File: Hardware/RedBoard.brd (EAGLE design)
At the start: 68.6 x 58.4 mm, 85 parts, among them IC3 LM1117, J2 ISP, J3 5.5x2.1mm Barrel, J4 QWIIC_RIGHT_ANGLE, J5 USB Female Type C Connector, Q1 20V/4.2A/52mΩ/1.4W, Q2 310mA/60V/1.6Ω, Q3 310mA/60V/1.6Ω, U3 3.3V, U4 ATMEGA328P_TQFP, U5 CH340C, Y1 16MHz

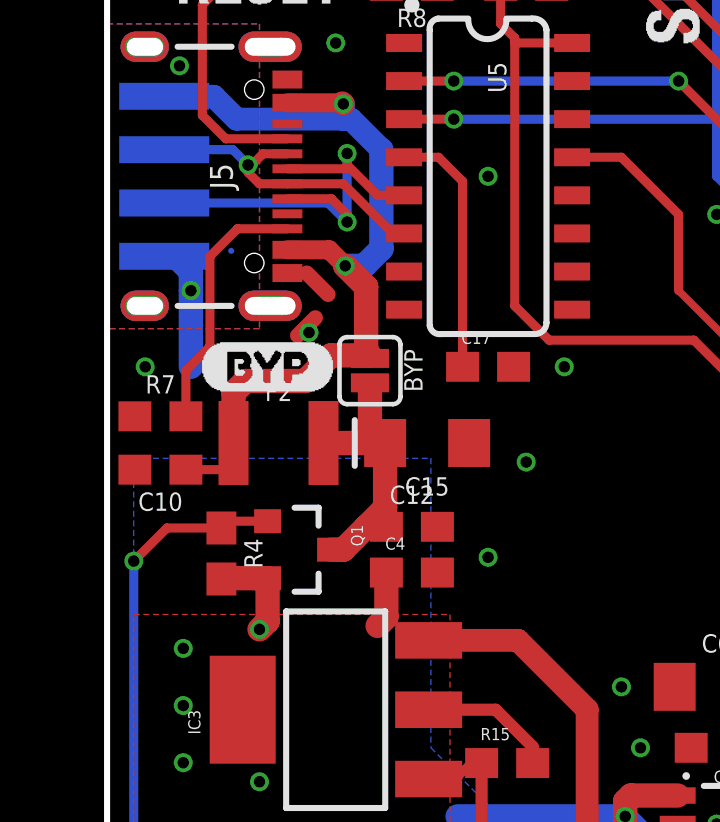
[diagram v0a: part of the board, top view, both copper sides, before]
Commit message: Go through DRC errors
Updated power MOSFET to be capable of 4.2A
Broke out A6 and A7 pins to headers
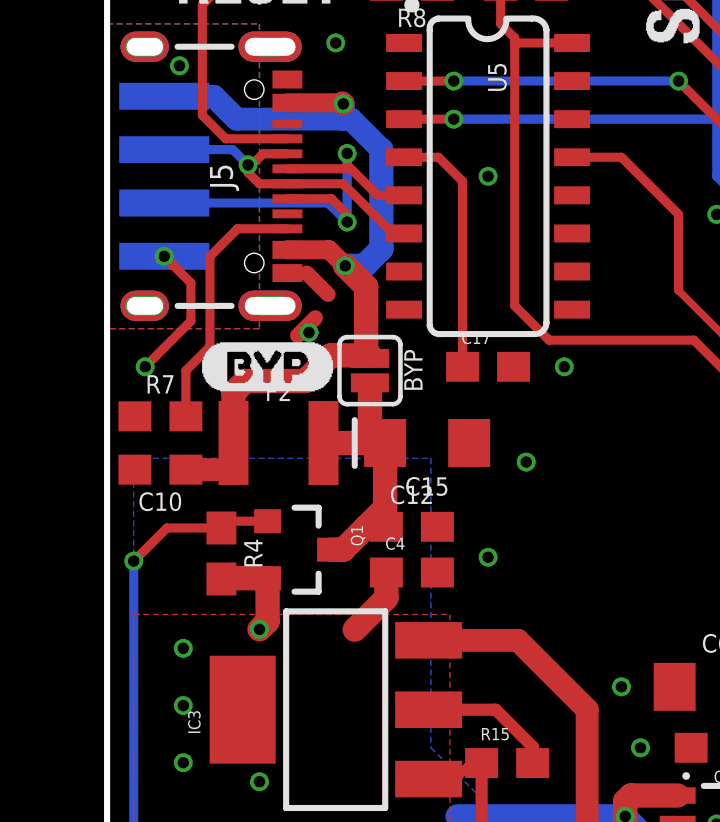
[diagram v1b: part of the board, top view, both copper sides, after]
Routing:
- net GND: track 18.7 -> 19.2 mm
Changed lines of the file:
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@@
 <wire x1="3.837" y1="28.514" x2="3.81" y2="28.487" width="0.8128" layer="1"/>
 <wire x1="5.35" y1="28.514" x2="5.35" y2="27.079" width="0.8128" layer="1"/>
-<wire x1="9.31" y1="28.702" x2="9.31" y2="27.217" width="0.8128" layer="1"/>
-<wire x1="9.31" y1="27.217" x2="9.017" y2="26.924" width="0.8128" layer="1"/>
+<wire x1="9.31" y1="28.702" x2="9.31" y2="27.852" width="0.8128" layer="1"/>
+<wire x1="9.31" y1="27.852" x2="8.255" y2="26.797" width="0.8128" layer="1"/>
 <via x="31.75" y="5.08" extent="1-16" drill="0.381"/>
 <contactref element="S2" pad="3"/>
@@
 <contactref element="S1" pad="2"/>
 <contactref element="JP14" pad="GND"/>
-<via x="1.27" y="35.56" extent="1-16" drill="0.381"/>
 <via x="20.32" y="20.32" extent="1-16" drill="0.381"/>
 <via x="22.86" y="20.32" extent="1-16" drill="0.381"/>
@@
 <via x="44.45" y="5.08" extent="1-16" drill="0.381"/>
 <via x="39.37" y="5.08" extent="1-16" drill="0.381"/>
-<wire x1="1.905" y1="39.243" x2="2.286" y2="39.243" width="0.8128" layer="16"/>
-<wire x1="2.286" y1="39.243" x2="2.794" y2="38.735" width="0.8128" layer="16"/>
-<wire x1="2.794" y1="38.735" x2="2.794" y2="38.1" width="0.8128" layer="16"/>
 <contactref element="JP15" pad="2"/>
 <contactref element="JP15" pad="3"/>
 <contactref element="JP12" pad="4"/>
-<wire x1="2.794" y1="38.1" x2="2.794" y2="35.56" width="0.8128" layer="16"/>
 <wire x1="26.416" y1="54.99" x2="26.416" y2="57.15" width="0.3048" layer="1"/>
 <wire x1="43.18" y1="3.43" x2="43.18" y2="1.27" width="0.762" layer="1"/>
@@
 <via x="35.56" y="22.479" extent="1-16" drill="0.381"/>
 <via x="34.29" y="25.146" extent="1-16" drill="0.381"/>
-<via x="2.794" y="38.1" extent="1-16" drill="0.381"/>
+<wire x1="1.27" y1="35.56" x2="1.397" y2="35.56" width="0.254" layer="1"/>
+<via x="1.905" y="39.243" extent="1-16" drill="0.381"/>
+<wire x1="1.905" y1="39.243" x2="2.794" y2="38.354" width="0.3048" layer="1"/>
+<wire x1="2.794" y1="37.084" x2="1.27" y2="35.56" width="0.3048" layer="1"/>
+<via x="1.27" y="35.56" extent="1-16" drill="0.381"/>
+<wire x1="2.794" y1="38.354" x2="2.794" y2="37.084" width="0.3048" layer="1"/>
 </signal>
 <signal name="AREF">
@@
 <wire x1="8.763" y1="35.8394" x2="8.763" y2="35.941" width="0.254" layer="1"/>
 <wire x1="8.763" y1="35.8394" x2="8.636" y2="35.9664" width="0.254" layer="1"/>
-<wire x1="2.628" y1="32.131" x2="3.937" y2="32.131" width="0.3048" layer="1"/>
-<wire x1="3.937" y1="32.131" x2="3.937" y2="32.742" width="0.3048" layer="1"/>
-<wire x1="3.937" y1="32.742" x2="4.215" y2="33.02" width="0.3048" layer="1"/>
+<wire x1="2.628" y1="32.131" x2="4.191" y2="32.131" width="0.762" layer="1"/>
+<wire x1="4.191" y1="32.131" x2="4.191" y2="32.996" width="0.762" layer="1"/>
+<wire x1="4.191" y1="32.996" x2="4.215" y2="33.02" width="0.762" layer="1"/>
 <wire x1="1.905" y1="44.577" x2="3.556" y2="44.577" width="0.762" layer="16"/>
 <wire x1="3.556" y1="44.577" x2="4.3184" y2="43.8146" width="0.762" layer="16"/>
@@
 <vertex x="0" y="36.83"/>
 </polygon>
-<wire x1="4.13791875" y1="39.42658125" x2="4.13391875" y2="39.42258125" width="0.2032" layer="16"/>
 <contactref element="J5" pad="SHLD4"/>
 <contactref element="J5" pad="SHLD3"/>
@@
 <contactref element="J5" pad="SHLD1"/>
 <via x="2.413" y="45.593" extent="1-16" drill="0.381"/>
-<wire x1="4.13791875" y1="39.42658125" x2="1.255" y2="37.592" width="0" layer="19" extent="16-16"/>
 </signal>
 <signal name="LV_SDA">
@@
 <wire x1="1.905" y1="42.799" x2="4.191" y2="42.799" width="0.3048" layer="16"/>
 <wire x1="4.191" y1="42.799" x2="4.699" y2="42.291" width="0.3048" layer="16"/>
-<wire x1="6.342" y1="41.66" x2="6.346" y2="41.656" width="0.254" layer="1"/>
+<wire x1="5.076" y1="41.66" x2="4.699" y2="42.037" width="0.3048" layer="1"/>
+<wire x1="6.01" y1="41.66" x2="5.076" y2="41.66" width="0.3048" layer="1"/>
 <wire x1="6.01" y1="41.66" x2="7.87" y2="41.66" width="0.3048" layer="1"/>
-<wire x1="6.01" y1="41.66" x2="5.076" y2="41.66" width="0.3048" layer="1"/>
-<wire x1="5.076" y1="41.66" x2="4.699" y2="42.037" width="0.3048" layer="1"/>
-<wire x1="6.01" y1="41.66" x2="6.342" y2="41.66" width="0" layer="19" extent="1-1"/>
 </signal>
 <signal name="D+">

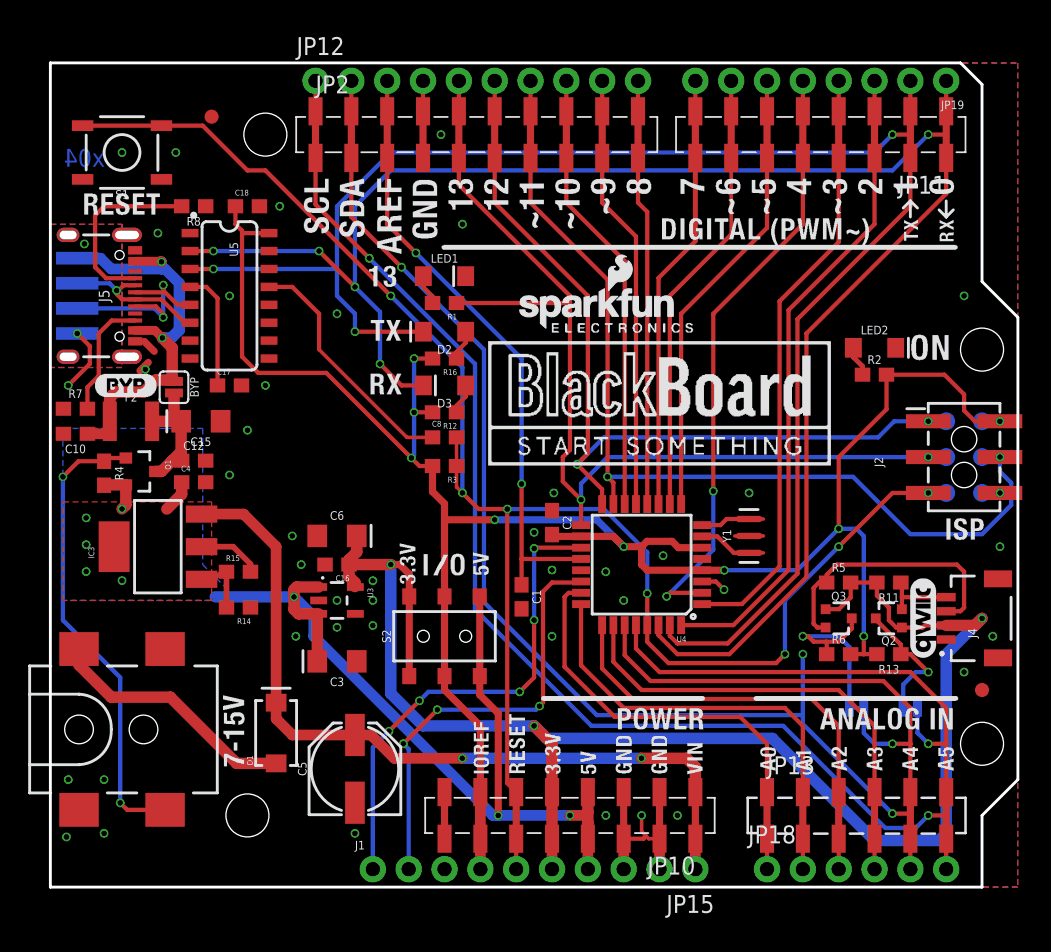
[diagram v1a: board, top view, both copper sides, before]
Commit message: Update silkscreen to vector buzzard labels
Working on making logo vector
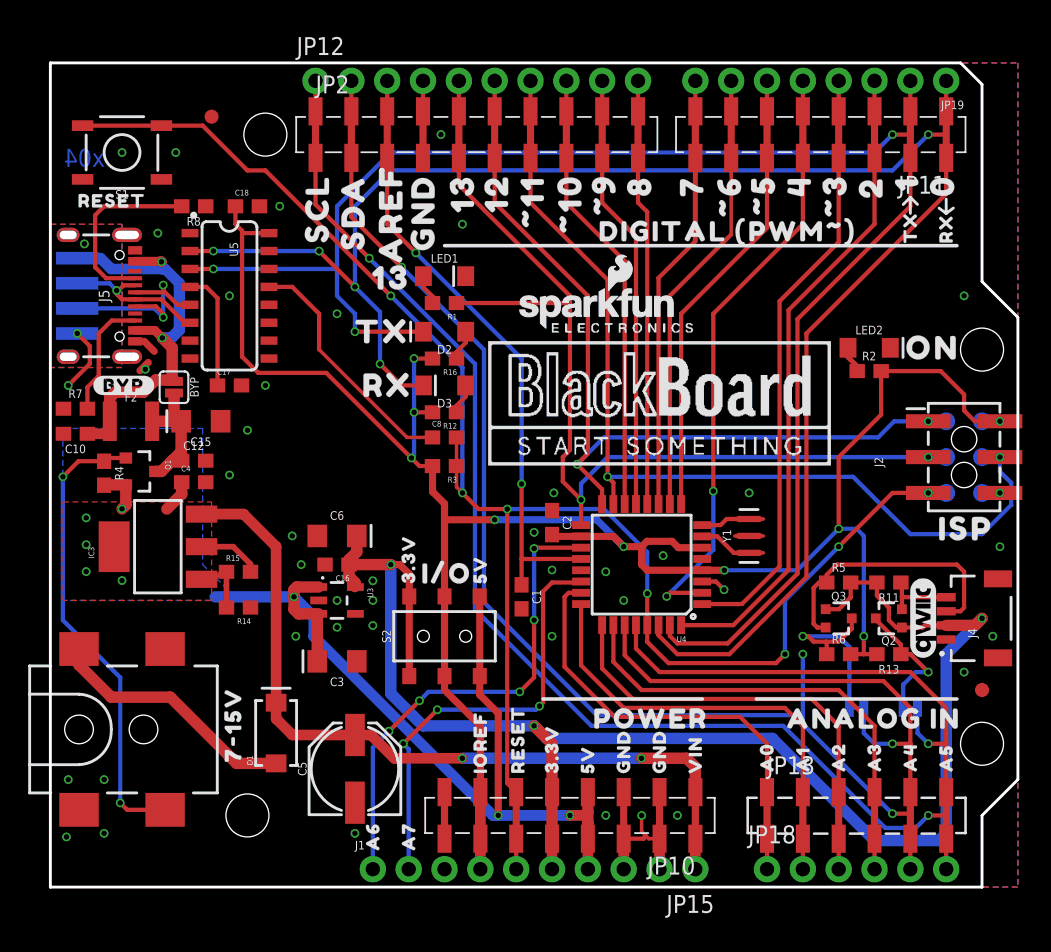
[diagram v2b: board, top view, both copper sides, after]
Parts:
- added U$100, U$21: (no value), output:_GND0
- added U$13, U$50, U$96: (no value), output:RESET0
- added U$14: (no value), output:#BYP#0
- added U$17: (no value), output:7#15V0
- added U$18, U$81: (no value), output:SCL0
- added U$19, U$80: (no value), output:SDA0
- added U$20, U$79: (no value), output:AREF0
- added U$22, U$77: (no value), output:130
- added U$23, U$76: (no value), output:120
- added U$24: (no value), output:#110
- added U$25: (no value), output:#100
- added U$26: (no value), output:#90
- added U$27, U$72: (no value), output:80
- added U$28, U$71: (no value), output:70
- added U$29: (no value), output:#60
- added U$30: (no value), output:#50
- added U$31: (no value), output:40
- added U$32: (no value), output:#30
- added U$33, U$66: (no value), output:20
- added U$34, U$65: (no value), output:10
- added U$35, U$64: (no value), output:00
- added U$36: (no value), output:TX0
- added U$37: (no value), output:RX0
- added U$38: (no value), output:DIGITAL_##PWM####_0
- added U$39: (no value), output:13_0
- added U$40: (no value), output:_TX0
- added U$41: (no value), output:_RX0
- added U$42: (no value), output:I#O0
- added U$43, U$51, U$95: (no value), output:3#3V0
- added U$44, U$52, U$94: (no value), output:5V0
- added U$45: (no value), output:ON0
- added U$46: (no value), output:ISP0
- added U$47: (no value), output:POWER0
- added U$48: (no value), output:ANALOG_IN0
- added U$49, U$97: (no value), output:IOREF0
- added U$53, U$54, U$92, U$93: (no value), output:GND0
- added U$55, U$91: (no value), output:VIN0
- added U$56, U$90: (no value), output:A00
- added U$57, U$89: (no value), output:A10
- added U$58, U$88: (no value), output:A20
- added U$59, U$87: (no value), output:A30
- added U$60, U$84: (no value), output:A40
- added U$61, U$85, U$86: (no value), output:A50
- added U$62, U$99: (no value), output:A60
- added U$63, U$98: (no value), output:A70
- added U$67: (no value), output:3#0
- added U$69: (no value), output:5#0
- added U$70: (no value), output:6#0
- added U$73: (no value), output:9#0
- added U$74: (no value), output:100
- added U$75: (no value), output:110
- added U$82: (no value), output:MADE_IN0
- added U$83: (no value), output:THE_USA0
- U$10: device buzzard_labels (14):D#4 -> output:G0
- U$11: device buzzard_labels (13):G1 -> output:A40
- U$12: device buzzard_labels (13):V0 -> output:D#0
- U$2: device buzzard_labels (14):D#3 -> output:_D#0
- U$4: device madeinusa:MADEINUSA#PNG -> output:V0
- U$68: device buzzard_labels (13):BYP0 -> output:40
- moved U$11 58.9 mm to (58.9, 14.5)
- moved U$68 54.7 mm to (53.3, 57.1), flipped to the bottom, turned to 270 degrees
- moved U$4 54.4 mm to (5.21, 44.6)
- moved U$12 3.58 mm to (5.84, 41.0)
- moved U$10 3.57 mm to (5.21, 39.2)
- moved U$2 1.85 mm to (6.10, 42.8)
- moved R2 0.46 mm to (58.0, 36.6)
- moved LED2 0.38 mm to (58.0, 38.2)
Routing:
- net VCC: track 146.6 -> 147.1 mm

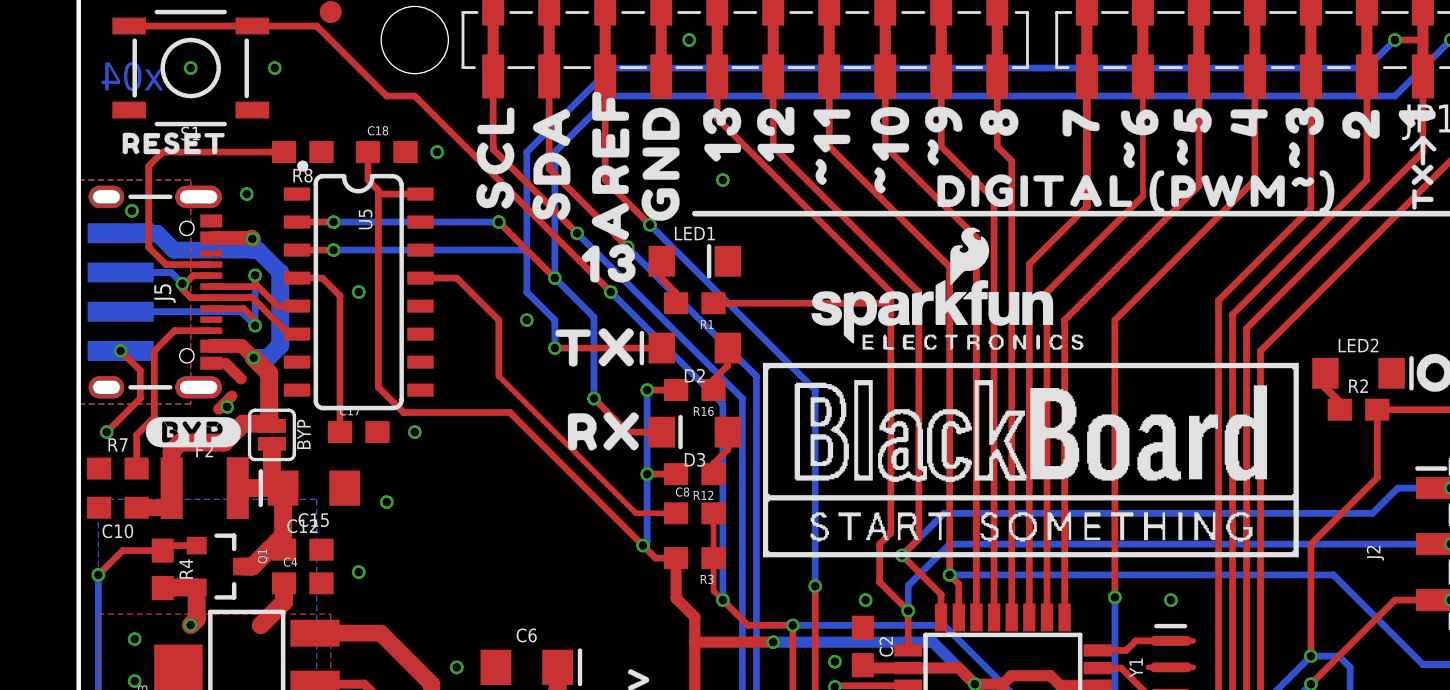
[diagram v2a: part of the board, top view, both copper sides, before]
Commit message: Finished vectorizing redboard logo. Updated board files
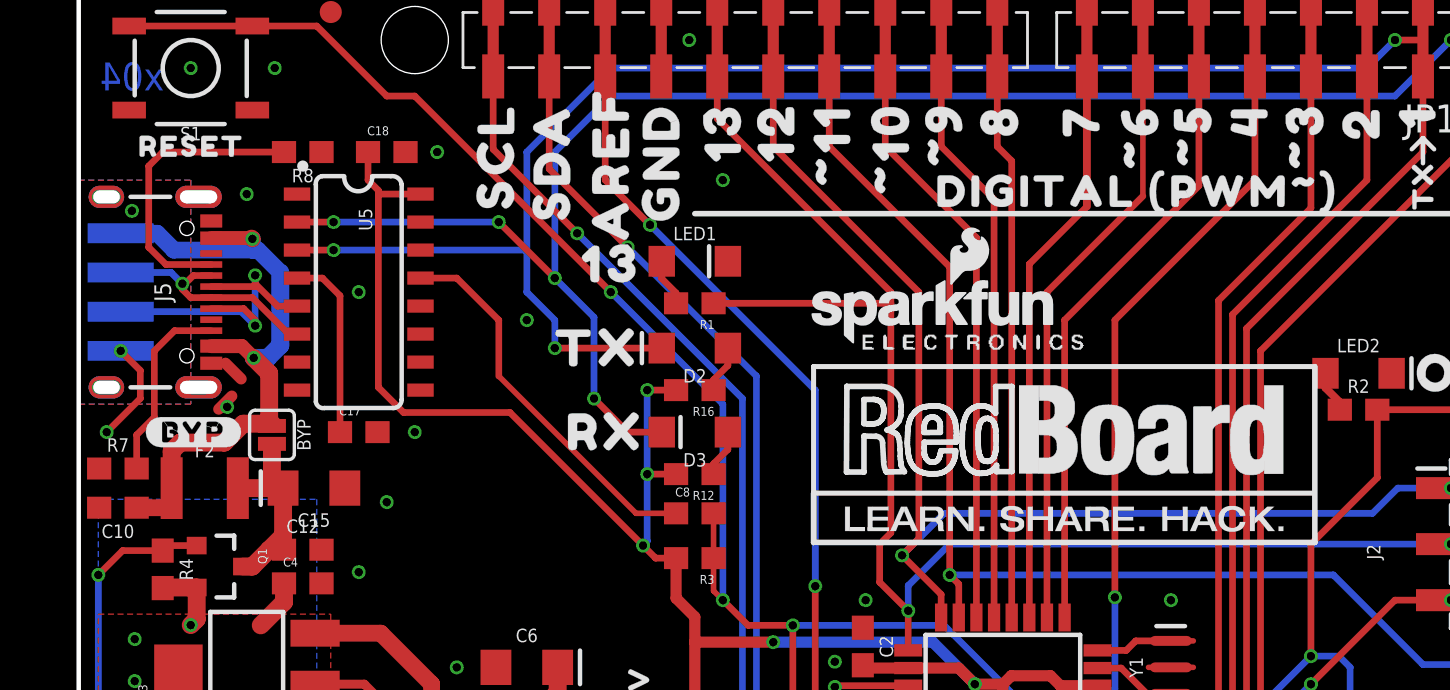
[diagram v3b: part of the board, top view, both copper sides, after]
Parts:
- removed U$3: (no value), blackboardlogo:BLACKBOARDLOGO#PNG
- added U$78: REDBOARD_LOGO, redboard_logo:REDBOARD_LOGO
- U$1: value (none) -> REDBOARD_LOGO; device blackboardlogo:BLACKBOARDLOGO#PNG -> redboard_logo:REDBOARD_LOGO
- moved U$1 21.5 mm to (63.0, 42.7), flipped to the bottom
- moved U$13 0.77 mm to (2.03, 48.5)
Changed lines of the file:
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@@
 <attribute name="VALUE" x="55.88" y="15.748" size="0.6096" layer="27" font="vector" ratio="15" align="top-center"/>
 </element>
-<element name="U$1" library="blackboardlogo" package="BLACKBOARDLOGO#PNG" value="" x="43.18" y="34.29" smashed="yes"/>
-<element name="U$3" library="blackboardlogo" package="BLACKBOARDLOGO#PNG" value="" x="50.8" y="46.99" smashed="yes" rot="MR0"/>
 <element name="J5" library="SparkFun-Connectors" package="USB-C-16P-2LAYER-PADS" value="USB Female Type C Connector" x="6.35" y="41.91" smashed="yes" rot="R270">
 <attribute name="NAME" x="3.81" y="41.91" size="0.762" layer="25" rot="R270" align="center"/>
@@
 <attribute name="VALUE" x="21.59" y="-0.762" size="0.6096" layer="27" font="vector" ratio="20"/>
 </element>
-<element name="U$13" library="output" package="RESET0" value="" x="1.27" y="48.641" smashed="yes"/>
+<element name="U$13" library="output" package="RESET0" value="" x="2.032" y="48.514" smashed="yes"/>
 <element name="U$14" library="output" package="#BYP#0" value="" x="3.048" y="35.56" smashed="yes"/>
 <element name="U$17" library="output" package="7#15V0" value="" x="12.954" y="8.001" smashed="yes" rot="R90"/>
@@
 <element name="U$100" library="output" package="_GND0" value="" x="26.416" y="43.307" smashed="yes" rot="R90"/>
 <element name="U$21" library="output" package="_GND0" value="" x="26.416" y="57.658" smashed="yes" rot="MR270"/>
+<element name="U$78" library="redboard_logo" package="REDBOARD_LOGO" value="REDBOARD_LOGO" x="33.274" y="30.353" smashed="yes"/>
+<element name="U$1" library="redboard_logo" package="REDBOARD_LOGO" value="REDBOARD_LOGO" x="62.992" y="42.672" smashed="yes" rot="MR0"/>
 </elements>
 <signals>
